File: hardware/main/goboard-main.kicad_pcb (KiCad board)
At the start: 2 copper layers, 304.7 x 135.9 mm, 184 parts, among them J1 USB_C_Receptacle_USB2.0, J2 Conn_02x05_Top_Bottom, J3 Conn_01x01, Q1 SSM3J338R, Q2 BCP53, Q3 SSM3J338R, Q4 BC817, Q5 SSM3J338R, Q6 BC807, Q7 BC817, Q8 BC817, SW1 Esc, SW10 a, SW12 Fn, SW13 F2, SW14 2, SW15 w, SW16 s, SW17 z, SW18 Tux, SW19 F3, SW2 F1, SW20 3, SW21 e, SW22 d, SW23 c, SW24 Alt, SW25 F4, SW26 4, SW27 r, SW28 f, SW29 v, SW3 tilde, SW30 SW_DP3T, SW31 F5, SW32 5, SW33 t, SW34 g, SW35 b, SW36 F6, SW37 6, SW38 y, SW39 h, SW4 Tab, SW40 n, SW41 F7, SW42 7, SW43 u, SW44 j, SW45 m, SW46 Space, SW47 F8, SW48 8, SW49 i, SW5 Caps Lock, SW50 k, SW51 comma, SW52 F9, SW53 9, SW54 o, SW55 l, SW56 dot, SW57 F10, SW58 0, SW59 p, SW6 Shift, SW60 semicolon, SW61 slash, SW62 Alt Gr, SW63 F11, SW64 minus, SW65 sq br open, SW66 apostrophe, SW67 Menu, SW68 F12, SW69 equal, SW7 Ctrl, SW70 sq br close, SW71 backslash, SW72 Shift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

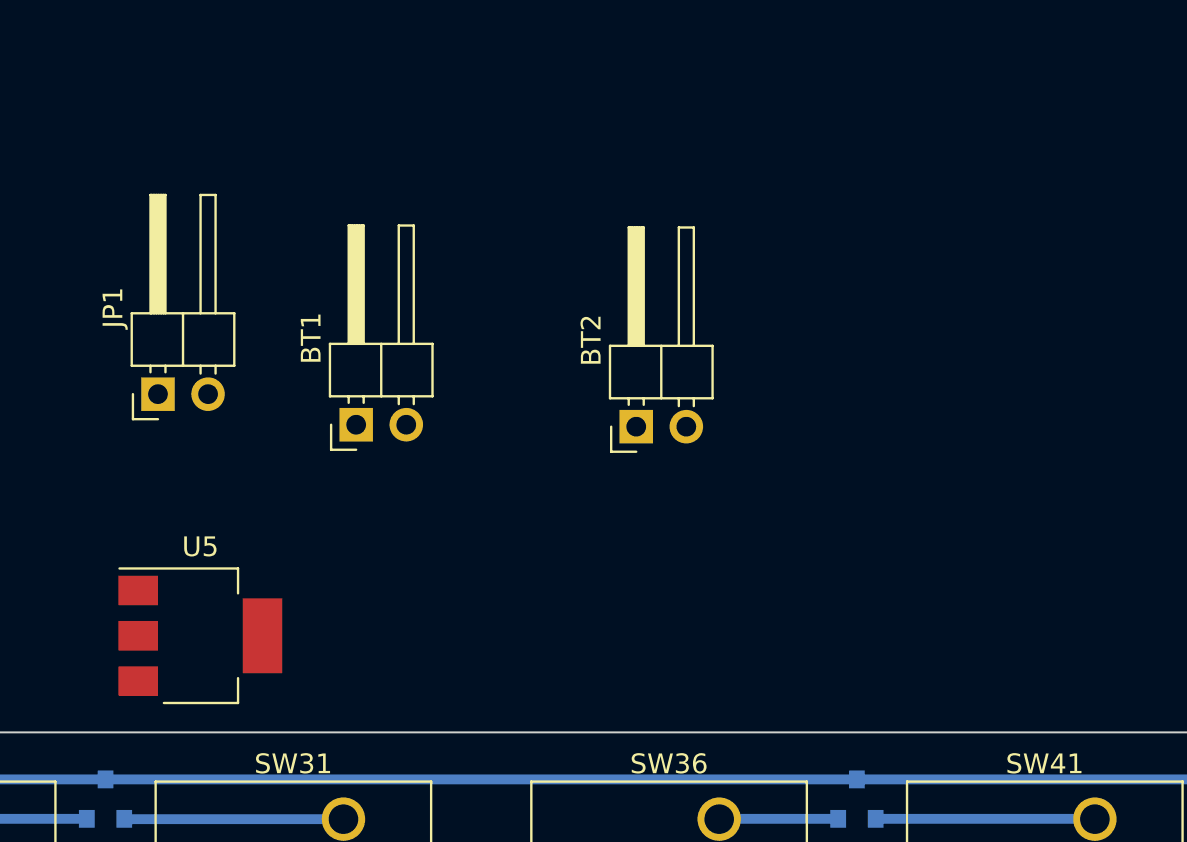
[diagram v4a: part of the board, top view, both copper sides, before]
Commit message: Assign footprints
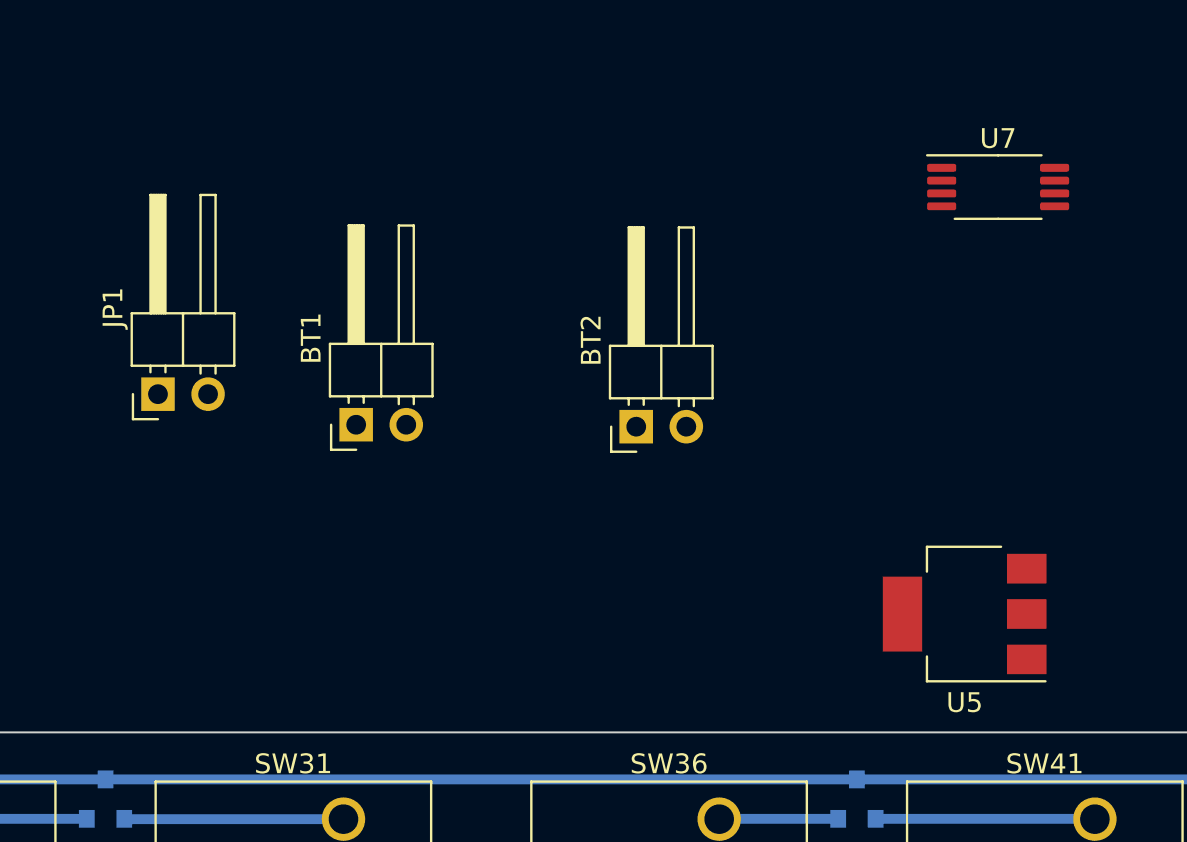
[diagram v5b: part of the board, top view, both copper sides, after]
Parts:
- added U7: LM358, Package_SO:TSSOP-8_4.4x3mm_P0.65mm, F.Cu at (178.4, 44.1)
- moved U5 38.8 mm to (176.8, 65.8), turned to 180 degrees
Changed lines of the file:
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@@
   (net 204 "unconnected-(U4-Pad7)")
   (net 205 "unconnected-(U4-Pad10)")
+  (net 206 "Net-(U7-Pad6)")
   (footprint "footprints:SW_Cherry_MX_1.00u_PCB" (layer "F.Cu")
     (at 269.08125 114.3)
@@
       (net 124 "Net-(SW61-Pad2)") (pinfunction "2"))
     (model "${KIPRJMOD}/../3dpackages/Button_Switch_Keyboard.3dshapes/SW_Cherry_MX_1.00u_PCB.wrl"
+      (offset (xyz 0 0 0))
+      (scale (xyz 1 1 1))
+      (rotate (xyz 0 0 0))
+    )
+  )
+  (footprint "Package_SO:TSSOP-8_4.4x3mm_P0.65mm" (layer "F.Cu")
+    (at 178.45 44.15)
+    (descr "TSSOP, 8 Pin (JEDEC MO-153 Var AA https://www.jedec.org/document_search?search_api_views_fulltext=MO-153), generated with kicad-footprint-generator ipc_gullwing_generator.py")
+    (tags "TSSOP SO")
+    (property "Dateiname Blatt" "power.kicad_sch")
+    (property "Mouser" "595-LM358PW ")
+    (property "Part Name" "LM358PW")
+    (property "Schaltplanname" "Power Supply")
+    (attr smd)
+    (fp_text reference "U7" (at 0 -2.45) (layer "F.SilkS")
+      (effects (font (size 1 1) (thickness 0.15)))
+    )
+    (fp_text value "LM358" (at 0 2.45) (layer "F.Fab")
+      (effects (font (size 1 1) (thickness 0.15)))
+    )
+    (fp_text user "${REFERENCE}" (at 0 0) (layer "F.Fab")
+      (effects (font (size 1 1) (thickness 0.15)))
+    )
+    (fp_line (start 0 -1.61) (end -3.6 -1.61) (layer "F.SilkS") (width 0.12))
+    (fp_line (start 0 -1.61) (end 2.2 -1.61) (layer "F.SilkS") (width 0.12))
+    (fp_line (start 0 1.61) (end -2.2 1.61) (layer "F.SilkS") (width 0.12))
+    (fp_line (start 0 1.61) (end 2.2 1.61) (layer "F.SilkS") (width 0.12))
+    (fp_line (start 3.85 -1.75) (end -3.85 -1.75) (layer "F.CrtYd") (width 0.05))
+    (fp_line (start 3.85 1.75) (end 3.85 -1.75) (layer "F.CrtYd") (width 0.05))
+    (fp_line (start -3.85 1.75) (end 3.85 1.75) (layer "F.CrtYd") (width 0.05))
+    (fp_line (start -3.85 -1.75) (end -3.85 1.75) (layer "F.CrtYd") (width 0.05))
+    (fp_line (start -2.2 1.5) (end -2.2 -0.75) (layer "F.Fab") (width 0.1))
+    (fp_line (start -1.45 -1.5) (end 2.2 -1.5) (layer "F.Fab") (width 0.1))
+    (fp_line (start -2.2 -0.75) (end -1.45 -1.5) (layer "F.Fab") (width 0.1))
+    (fp_line (start 2.2 1.5) (end -2.2 1.5) (layer "F.Fab") (width 0.1))
+    (fp_line (start 2.2 -1.5) (end 2.2 1.5) (layer "F.Fab") (width 0.1))
+    (pad "1" smd roundrect (at -2.8625 -0.975) (locked) (size 1.475 0.4) (layers "F.Cu" "F.Paste" "F.Mask") (roundrect_rratio 0.25)
+      (net 193 "Net-(Q2-Pad1)"))
+    (pad "2" smd roundrect (at -2.8625 -0.325) (locked) (size 1.475 0.4) (layers "F.Cu" "F.Paste" "F.Mask") (roundrect_rratio 0.25)
+      (net 191 "Net-(Q2-Pad3)") (pinfunction "-"))
+    (pad "3" smd roundrect (at -2.8625 0.325) (locked) (size 1.475 0.4) (layers "F.Cu" "F.Paste" "F.Mask") (roundrect_rratio 0.25)
+      (net 145 "Net-(R10-Pad2)") (pinfunction "+"))
+    (pad "4" smd roundrect (at -2.8625 0.975) (locked) (size 1.475 0.4) (layers "F.Cu" "F.Paste" "F.Mask") (roundrect_rratio 0.25)
+      (net 47 "GND") (pinfunction "V-"))
+    (pad "5" smd roundrect (at 2.8625 0.975) (locked) (size 1.475 0.4) (layers "F.Cu" "F.Paste" "F.Mask") (roundrect_rratio 0.25)
+      (net 144 "Net-(R8-Pad1)") (pinfunction "+"))
+    (pad "6" smd roundrect (at 2.8625 0.325) (locked) (size 1.475 0.4) (layers "F.Cu" "F.Paste" "F.Mask") (roundrect_rratio 0.25)
+      (net 206 "Net-(U7-Pad6)") (pinfunction "-"))
+    (pad "7" smd roundrect (at 2.8625 -0.325) (locked) (size 1.475 0.4) (layers "F.Cu" "F.Paste" "F.Mask") (roundrect_rratio 0.25)
+      (net 206 "Net-(U7-Pad6)"))
+    (pad "8" smd roundrect (at 2.8625 -0.975) (locked) (size 1.475 0.4) (layers "F.Cu" "F.Paste" "F.Mask") (roundrect_rratio 0.25)
+      (net 31 "+5V") (pinfunction "V+"))
+    (model "${KICAD6_3DMODEL_DIR}/Package_SO.3dshapes/TSSOP-8_4.4x3mm_P0.65mm.wrl"
       (offset (xyz 0 0 0))
       (scale (xyz 1 1 1))
@@
   )
   (footprint "Package_TO_SOT_SMD:SOT-223-3_TabPin2" (layer "F.Cu")
-    (at 138 66.9)
+    (at 176.75 65.8 180)
     (descr "module CMS SOT223 4 pins")
     (tags "CMS SOT")
@@
     (fp_line (start -0.85 -3.35) (end 1.85 -3.35) (layer "F.Fab") (width 0.1))
     (fp_line (start -1.85 3.35) (end 1.85 3.35) (layer "F.Fab") (width 0.1))
-    (pad "1" smd rect (at -3.15 -2.3) (locked) (size 2 1.5) (layers "F.Cu" "F.Paste" "F.Mask")
+    (pad "1" smd rect (at -3.15 -2.3 180) (locked) (size 2 1.5) (layers "F.Cu" "F.Paste" "F.Mask")
       (net 47 "GND") (pinfunction "GND"))
-    (pad "2" smd rect (at -3.15 0) (locked) (size 2 1.5) (layers "F.Cu" "F.Paste" "F.Mask")
+    (pad "2" smd rect (at -3.15 0 180) (locked) (size 2 1.5) (layers "F.Cu" "F.Paste" "F.Mask")
       (net 128 "+3V3") (pinfunction "VO"))
-    (pad "2" smd rect (at 3.15 0) (locked) (size 2 3.8) (layers "F.Cu" "F.Paste" "F.Mask")
+    (pad "2" smd rect (at 3.15 0 180) (locked) (size 2 3.8) (layers "F.Cu" "F.Paste" "F.Mask")
       (net 128 "+3V3") (pinfunction "VO"))
-    (pad "3" smd rect (at -3.15 2.3) (locked) (size 2 1.5) (layers "F.Cu" "F.Paste" "F.Mask")
+    (pad "3" smd rect (at -3.15 2.3 180) (locked) (size 2 1.5) (layers "F.Cu" "F.Paste" "F.Mask")
       (net 31 "+5V") (pinfunction "VI"))
     (model "${KICAD6_3DMODEL_DIR}/Package_TO_SOT_SMD.3dshapes/SOT-223.wrl"

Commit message: WIP: Design of PCB
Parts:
- removed C1: 100nF, Capacitor_SMD:C_0603_1608Metric_Pad1.08x0.95mm_HandSolder
- removed C2: 4.7nF, Capacitor_SMD:C_0603_1608Metric_Pad1.08x0.95mm_HandSolder
- added R21: 0, Resistor_SMD:R_0603_1608Metric_Pad0.98x0.95mm_HandSolder, F.Cu at (132.5, 176.4)
- added SW11: SW_Push, Button_Switch_SMD:SW_SPST_CK_RS282G05A3, F.Cu at (210.5, 178.8)
- C4, C5, C6, U2, U3, U4: moved to B.Cu
- R1: value 0 -> DNP
- moved C4 196.7 mm to (110.4, 103.8), turned to 90 degrees
- moved U3 182.1 mm to (114.0, 100.2), turned to -90 degrees
- moved C7 145.9 mm to (210.5, 175.8), turned to 180 degrees
- moved J3 139.9 mm to (202.7, 171.9)
- moved R15 130.2 mm to (201.9, 69.0), turned to 90 degrees
- moved R17 128.5 mm to (199.4, 66.5), turned to 180 degrees
- moved R16 125.1 mm to (202.6, 61.3), turned to 180 degrees
- moved Q6 124.1 mm to (199.3, 69.2), turned to 90 degrees
- moved Q7 124.0 mm to (199.3, 62.2), turned to -90 degrees
- moved R18 123.5 mm to (199.4, 64.9)
- moved JP1 120.5 mm to (135.5, 175.1), turned to 0 degrees
- moved U2 72.2 mm to (332.8, 128.8), turned to 180 degrees
- moved BT1 68.4 mm to (79.2, 71.4), turned to 180 degrees
- moved C5 64.8 mm to (329.5, 124.5)
- moved C3 60.2 mm to (252.2, 71.1), turned to 180 degrees
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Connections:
- BT1 pad 2: /Power Supply/VMID -> /MCU/V_MID
- BT2 pad 1: /Power Supply/VMID -> /MCU/V_MID
- C4 pad 2: Net-(C4-Pad2) -> GND
- C5 pad 1: Net-(C5-Pad1) -> /VCC_SW
- C6 pad 1: Net-(C6-Pad1) -> /VCC_SW
- JP1 pad 1: +BATT -> Net-(JP1-Pad1)
- Q1 pad 3: +BATT -> Net-(JP1-Pad1)
- Q8 pad 3: /Power Supply/~USB_CONN -> /MCU/~USB_CONN
- R13 pad 2: /Power Supply/CHARGE -> /MCU/CHARGE
- R15 pad 1: /Power Supply/~BAL_HIGH -> /MCU/~BAL_HIGH
- R16 pad 1: /Power Supply/BAL_LOW -> /MCU/BAL_LOW
- R17 pad 2: /Power Supply/VMID -> /MCU/V_MID
- R18 pad 1: /Power Supply/VMID -> /MCU/V_MID
- R20 pad 1: /Power Supply/~USB_CONN -> /MCU/~USB_CONN
- U1 pad 2: unconnected-(U1-Pad2) -> /MCU/BAL_LOW
- U1 pad 23: /MCU/D- -> /USB_D-
- U1 pad 24: /MCU/D+ -> /USB_D+
- U1 pad 4: unconnected-(U1-Pad4) -> /MCU/~BAL_HIGH
- U1 pad 5: unconnected-(U1-Pad5) -> /MCU/~USB_CONN
- U1 pad 7: unconnected-(U1-Pad7) -> /MCU/V_MID
- U1 pad 8: unconnected-(U1-Pad8) -> /MCU/CHARGE
- U2 pad 1: Net-(D11-Pad3) -> Net-(D14-Pad3)
- U2 pad 15: Net-(D1-Pad3) -> unconnected-(U2-Pad15)
- U2 pad 16: Net-(C4-Pad2) -> /VCC_SW
- U2 pad 2: Net-(D12-Pad3) -> Net-(D1-Pad3)
- U2 pad 3: Net-(D10-Pad3) -> Net-(D15-Pad3)
- U2 pad 4: Net-(D15-Pad3) -> Net-(D10-Pad3)
- U2 pad 5: Net-(D14-Pad3) -> unconnected-(U2-Pad5)
- U2 pad 6: unconnected-(U2-Pad6) -> Net-(D12-Pad3)
- U2 pad 7: unconnected-(U2-Pad7) -> Net-(D11-Pad3)
- U3 pad 5: Net-(SW10-Pad2) -> Net-(SW1-Pad2)
- U3 pad 6: Net-(SW1-Pad2) -> Net-(SW10-Pad2)
- U3 pad 8: Net-(C5-Pad1) -> GND
- U4 pad 5: Net-(SW51-Pad2) -> Net-(SW45-Pad2)
- U4 pad 6: Net-(SW45-Pad2) -> Net-(SW51-Pad2)
- U4 pad 8: Net-(C6-Pad1) -> GND
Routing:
- net +BATT: track 0.00 -> 237.1 mm
- net Net-(JP1-Pad1): track 0.00 -> 222.5 mm
- net +3V3: track 0.00 -> 132.4 mm, vias 0 -> 9
- net /SWDIO: track 0.00 -> 91.5 mm, vias 0 -> 7
- net Net-(D12-Pad3): track 267.7 -> 180.2 mm
- net Net-(SW45-Pad2): track 86.5 -> 161.2 mm, vias 8 -> 10
- net Net-(SW1-Pad2): track 102.6 -> 176.8 mm, vias 0 -> 2
- net Net-(SW40-Pad2): track 86.2 -> 153.3 mm
- net Net-(D12-Pad1): track 64.5 -> 0.00 mm
- net Net-(D15-Pad3): track 236.4 -> 300.0 mm
- net Net-(SW78-Pad2): track 125.4 -> 68.0 mm
- net Net-(SW51-Pad2): track 86.6 -> 143.8 mm, vias 4 -> 6
- net Net-(SW10-Pad2): track 108.7 -> 165.6 mm, vias 7 -> 8
- net Net-(D14-Pad3): track 274.0 -> 325.1 mm
- net Net-(SW35-Pad2): track 115.4 -> 165.0 mm, vias 9 -> 10
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- added copper zone on F.Cu, net +3V3
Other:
- board size 304.7 x 135.9 mm -> 304.7 x 114.2 mm
- board text added: "TODO: Copper plane as big as possible on upper and lower side for: - U5 - Q2"

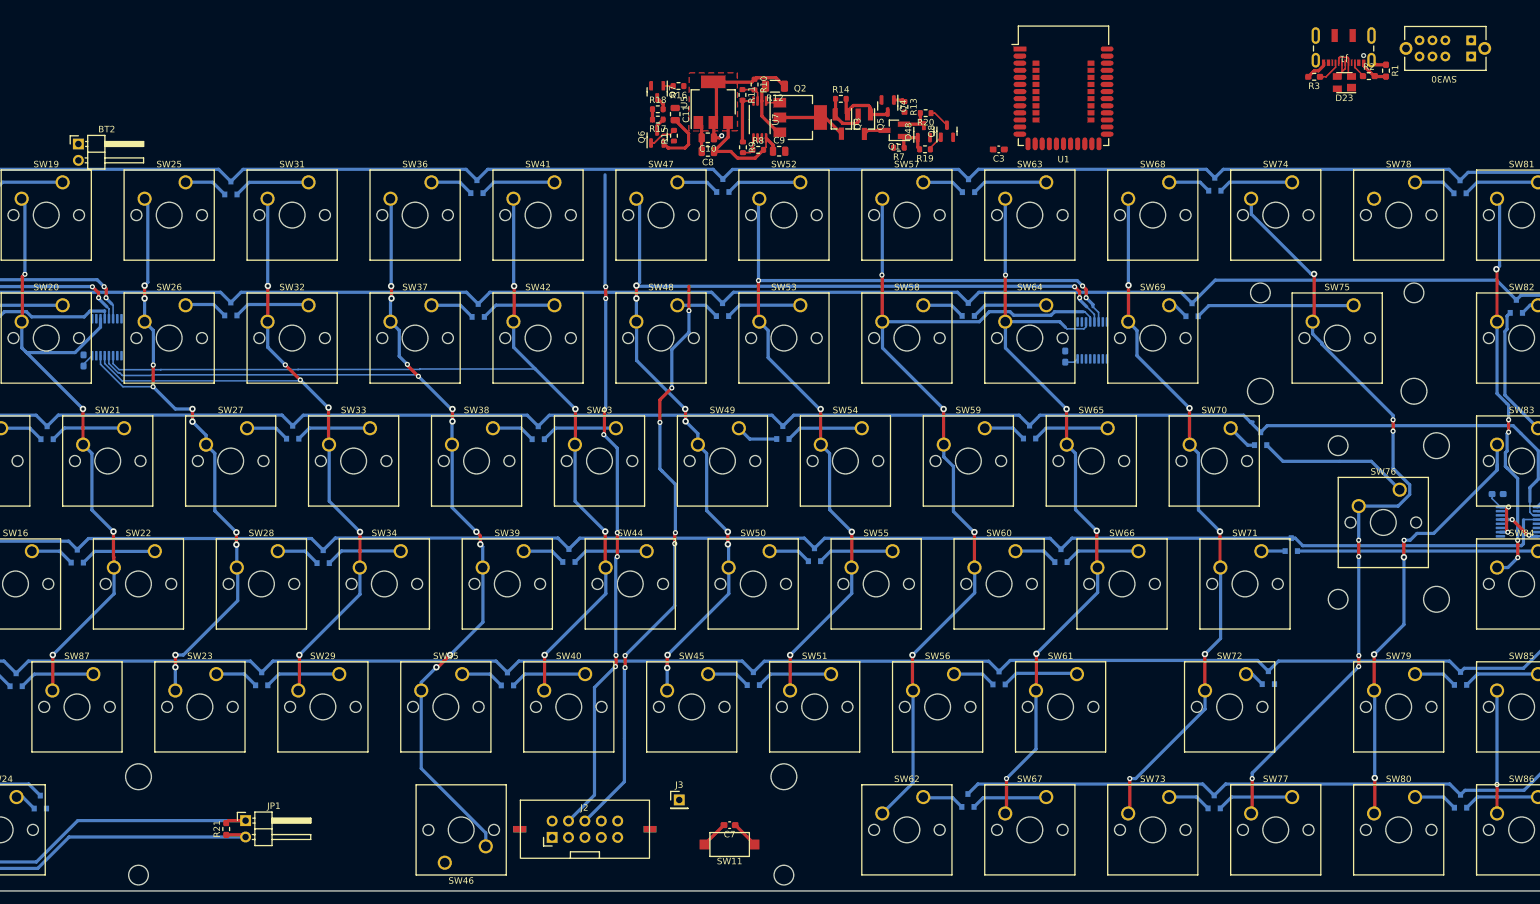
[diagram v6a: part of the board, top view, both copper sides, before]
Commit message: Route traces for the shift registers
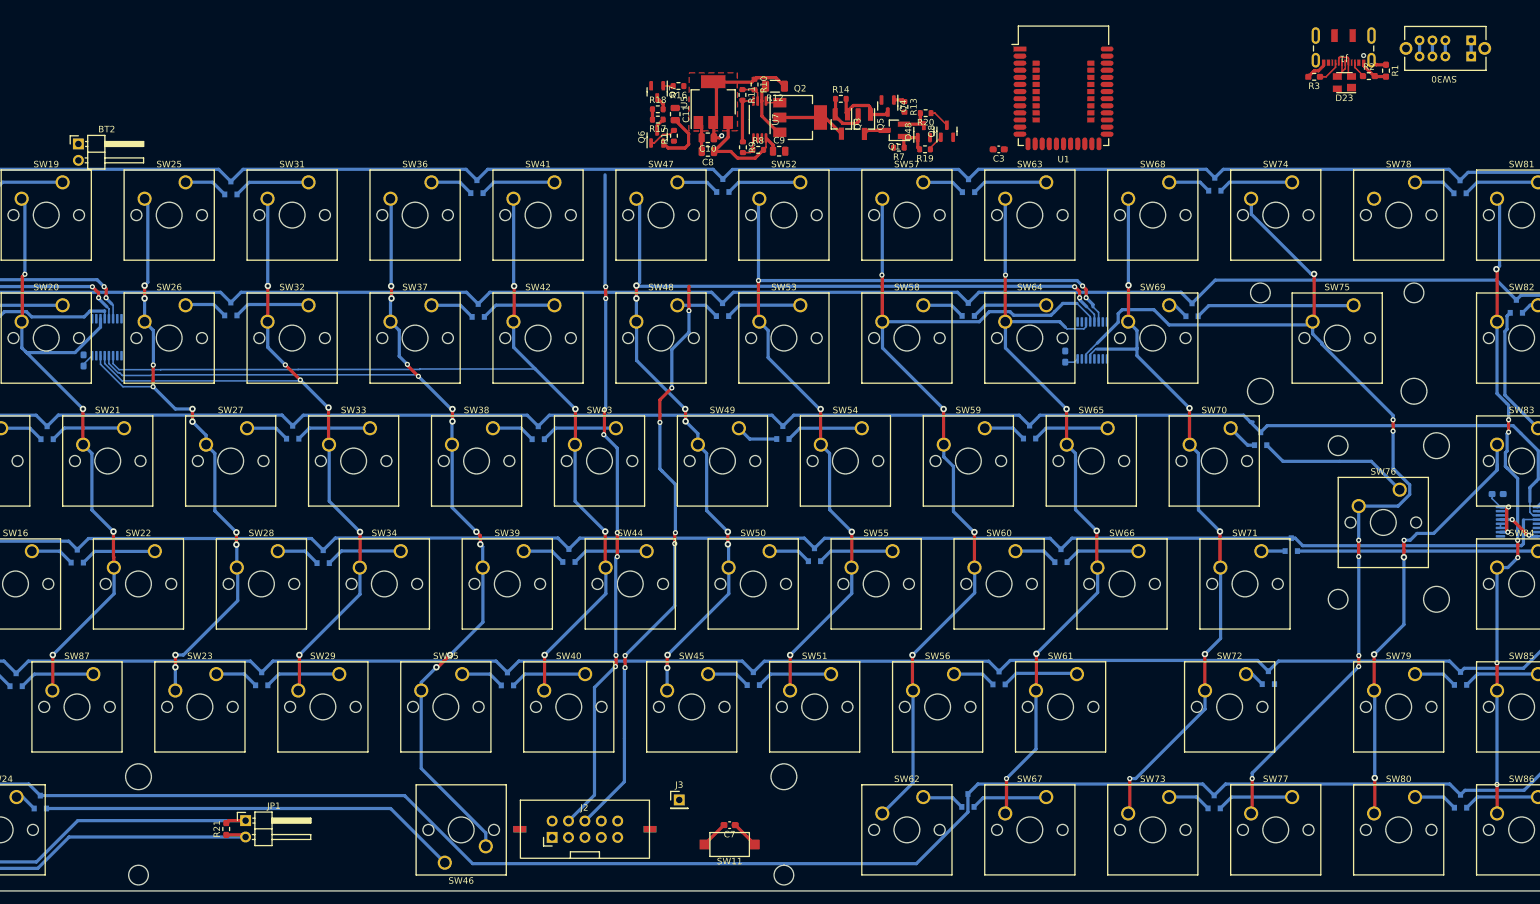
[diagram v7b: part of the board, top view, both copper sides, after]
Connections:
- SW74 pad 2: Net-(SW74-Pad2) -> Net-(U4-Pad14)
- SW75 pad 2: Net-(SW74-Pad2) -> Net-(U4-Pad14)
- SW76 pad 2: Net-(SW74-Pad2) -> Net-(U4-Pad14)
- SW77 pad 2: Net-(SW74-Pad2) -> Net-(U4-Pad14)
- U4 pad 13: Net-(SW74-Pad2) -> Net-(SW68-Pad2)
- U4 pad 14: Net-(SW68-Pad2) -> Net-(U4-Pad14)
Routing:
- net Net-(U4-Pad14): track 0.00 -> 160.4 mm, vias 0 -> 8
- net Net-(D12-Pad3): track 180.2 -> 334.4 mm
- net Net-(SW74-Pad2): track 119.7 -> 0.00 mm, vias 8 -> 0
- net Net-(D12-Pad1): track 0.00 -> 65.2 mm
- net Net-(SW81-Pad2): track 81.3 -> 100.4 mm, vias 6 -> 7
- net Net-(SW68-Pad2): track 107.7 -> 116.0 mm
- net /switch_usb_off: track 0.00 -> 2.50 mm
- net /switch_bt_2: track 0.00 -> 2.50 mm
- net /switch_bt_1: track 0.00 -> 2.50 mm
- net /VCC_SW: track 18.6 -> 21.1 mm
- net Net-(SW56-Pad2): track 141.8 -> 142.9 mm
- net /MCU/SPI_SCK: track 0.00 -> 0.65 mm
